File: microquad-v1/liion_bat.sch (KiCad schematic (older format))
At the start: 12 parts

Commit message: Double checked and hooked up connections for BLE Added Power and Pin 12 LED
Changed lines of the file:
@@
 $Descr A4 11693 8268
 encoding utf-8
-Sheet 5 7
+Sheet 5 8
 Title ""
 Date ""
@@
 $EndComp
 Wire Wire Line
-	5600 2750 5400 2750
-Wire Wire Line
-	5400 2750 5350 2750
+	5600 2750 5350 2750
 $Comp
 L C_Small Cbat?
@@
 $EndComp
 Wire Wire Line
-	5600 1800 5600 2250
-Wire Wire Line
-	5600 2250 5600 2750
+	5600 1800 5600 2750
 $Comp
 L GND #PWR019
@@
 $EndComp
 Wire Wire Line
-	5025 3800 5450 3800
-Wire Wire Line
-	5450 3800 5625 3800
+	5025 3800 5625 3800
 Wire Wire Line
 	5625 3800 5625 2950
@@
 	5100 3900 5100 3950
 Wire Wire Line
-	4900 4650 5425 4650
-Wire Wire Line
-	5425 4650 5450 4650
+	4900 4650 5450 4650
 Wire Wire Line
 	5450 4650 5450 3800
@@
 	4900 4850 4975 4850
 Wire Wire Line
-	4975 4850 4975 5025
-Wire Wire Line
-	4975 5025 4975 5075
+	4975 4850 4975 5075
 $Comp
 L R_Small Rbat?
@@
 	4000 4650 3925 4650
 Wire Wire Line
-	3925 4650 3925 4350
-Wire Wire Line
-	3925 4350 3700 4350
-Wire Wire Line
-	3700 4350 3500 4350
+	3925 4350 3925 4650
+Wire Wire Line
+	3500 4350 3925 4350
 $Comp
 L C_Small Cbat?
@@
 Connection ~ 3700 4350
 Wire Wire Line
-	3500 2675 3500 4350
-Wire Wire Line
-	3500 4350 3500 4500
+	3500 2675 3500 4500
 Wire Wire Line
 	3500 4700 3500 4850
@@
 	4250 3150 4250 2950
 Wire Wire Line
-	4250 2950 4375 2950
-Wire Wire Line
-	4375 2950 4450 2950
+	4250 2950 4450 2950
 $Comp
 L GND #PWR027

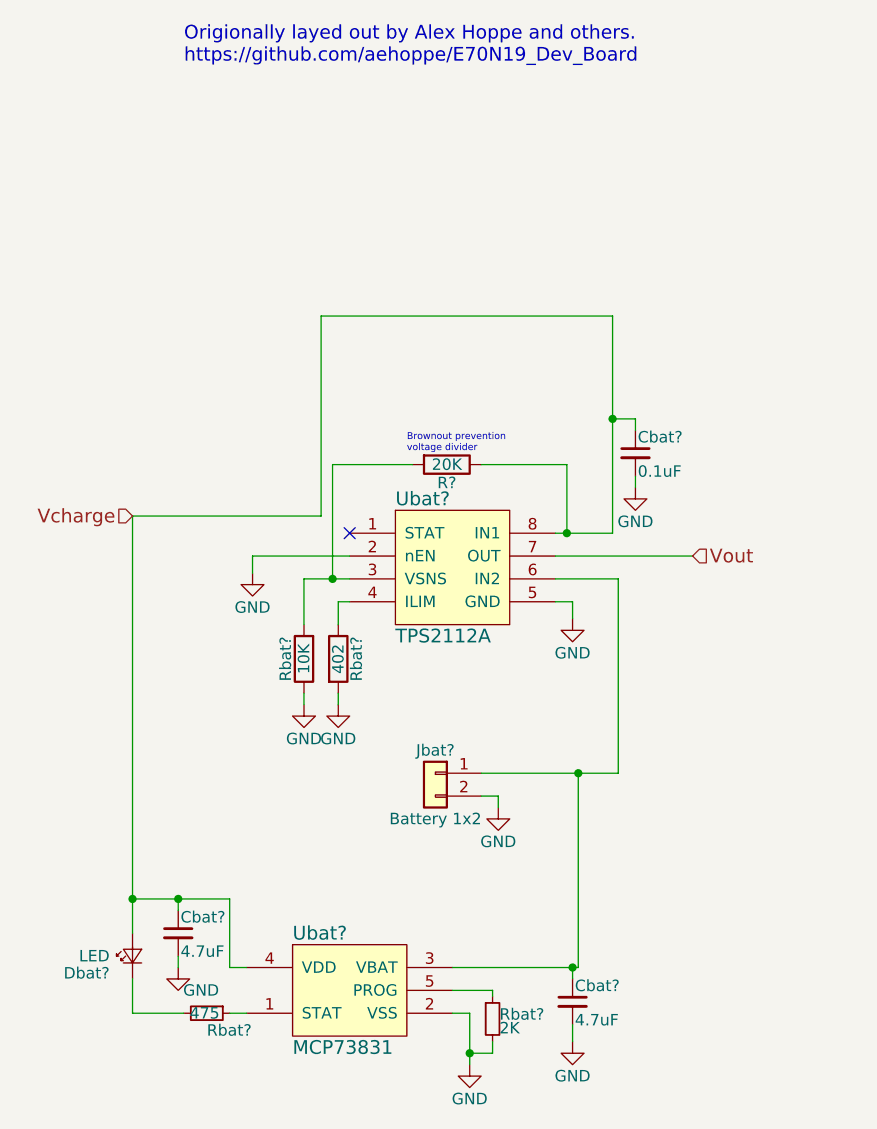
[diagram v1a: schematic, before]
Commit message: Switched battery and merged some more stuff
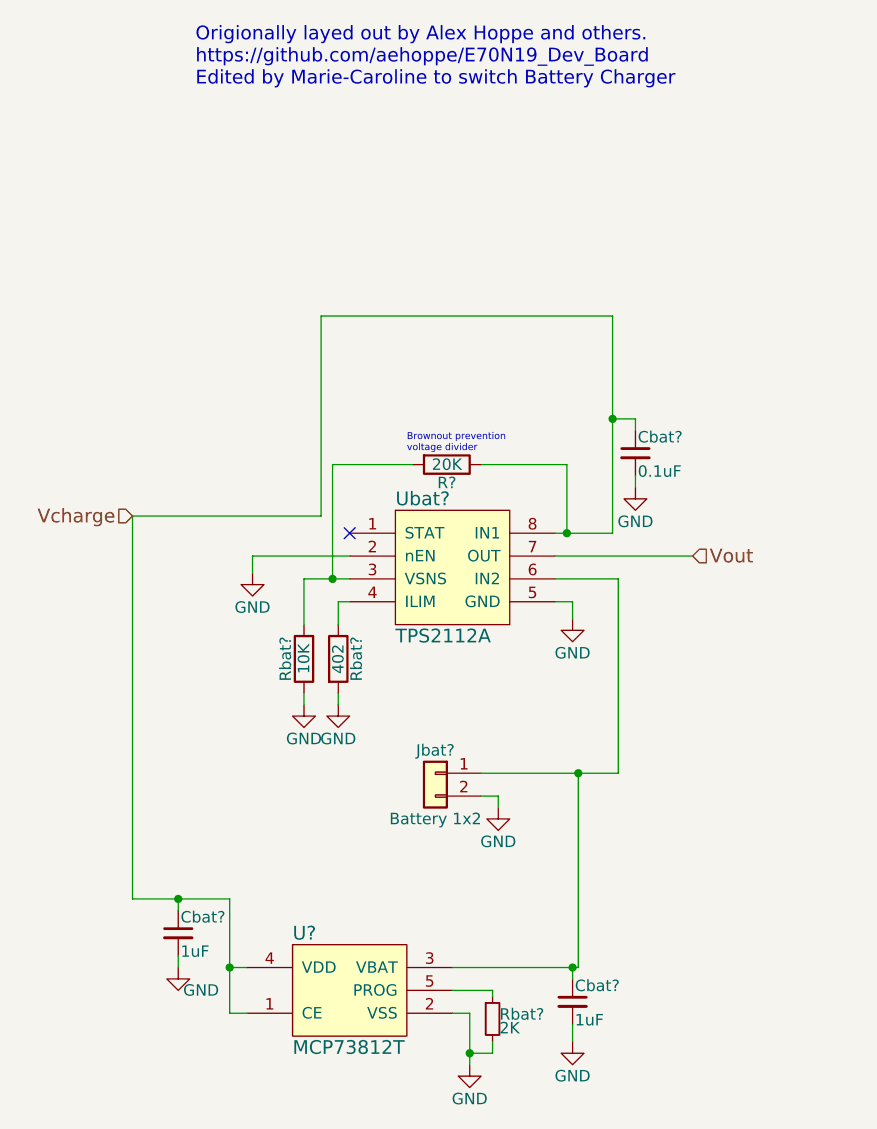
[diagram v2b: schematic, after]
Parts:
- removed Dbat?: LED, LEDs:LED_0805, symbol LED_Small
- removed Rbat?: 475, Resistors_SMD:R_0603, symbol R_Small
- removed Ubat?: MCP73831, TO_SOT_Packages_SMD:SOT-23-5, symbol MCP73831
- added U?: MCP73812T, symbol MCP73812T
- Cbat? (x2): value 4.7uF -> 1uF
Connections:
- net GND: now also U?.2 (VSS)
- net Vcharge: now also U?.1 (CE), U?.4 (VDD)
- net at Cbat?.1, Jbat?.1 (Pin_1), Ubat?.6 (IN2): now also U?.3 (VBAT)
- net at Rbat?.1: now also U?.5 (PROG)
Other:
- note added: "Origionally layed out by Alex Hoppe and others.\nhttps://github.com/aehoppe/E70N19_Dev_Board\nEdited by Marie-Caroline to switch Battery Charger"
- note removed: "Origionally layed out by Alex Hoppe and others.\nhttps://github.com/aehoppe/E70N19_Dev_Board"
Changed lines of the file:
@@
 $Descr A4 11693 8268
 encoding utf-8
-Sheet 5 8
+Sheet 10 8
 Title ""
 Date ""
@@
 U 1 1 59F538F1
 P 4900 2900
+AR Path="/59F6680F/59F538F1" Ref="Ubat?"  Part="1"
+AR Path="/59F56F7F/59F538F1" Ref="Ubat?"  Part="1"
 F 0 "Ubat?" H 4650 3200 60  0000 L CNN
 F 1 "TPS2112A" H 4650 2600 60  0000 L CNN
@@
 U 1 1 59F53938
 P 5700 2400
+AR Path="/59F6680F/59F53938" Ref="Cbat?"  Part="1"
+AR Path="/59F56F7F/59F53938" Ref="Cbat?"  Part="1"
 F 0 "Cbat?" H 5710 2470 50  0000 L CNN
 F 1 "0.1uF" H 5710 2320 50  0000 L CNN
@@
 U 1 1 59F53940
 P 5700 2550
+AR Path="/59F6680F/59F53940" Ref="#PWR019"  Part="1"
+AR Path="/59F56F7F/59F53940" Ref="#PWR019"  Part="1"
 F 0 "#PWR019" H 5700 2300 50  0001 C CNN
 F 1 "GND" H 5700 2400 50  0000 C CNN
@@
 U 1 1 59F5394A
 P 5425 3125
+AR Path="/59F6680F/59F5394A" Ref="#PWR020"  Part="1"
+AR Path="/59F56F7F/59F5394A" Ref="#PWR020"  Part="1"
 F 0 "#PWR020" H 5425 2875 50  0001 C CNN
 F 1 "GND" H 5425 2975 50  0000 C CNN
@@
 U 1 1 59F53953
 P 4400 3500
+AR Path="/59F6680F/59F53953" Ref="#PWR021"  Part="1"
+AR Path="/59F56F7F/59F53953" Ref="#PWR021"  Part="1"
 F 0 "#PWR021" H 4400 3250 50  0001 C CNN
 F 1 "GND" H 4400 3350 50  0000 C CNN
@@
 U 1 1 59F5395B
 P 4400 3300
+AR Path="/59F6680F/59F5395B" Ref="Rbat?"  Part="1"
+AR Path="/59F56F7F/59F5395B" Ref="Rbat?"  Part="1"
 F 0 "Rbat?" V 4480 3300 50  0000 C CNN
 F 1 "402" V 4400 3300 50  0000 C CNN
@@
 	4400 3050 4400 3150
 $Comp
-L MCP73831 Ubat?
-U 1 1 59F53965
-P 4450 4750
-F 0 "Ubat?" H 4200 5000 60  0000 L CNN
-F 1 "MCP73831" H 4200 4500 60  0000 L CNN
-F 2 "TO_SOT_Packages_SMD:SOT-23-5" H 4450 4750 60  0001 C CNN
-F 3 "" H 4450 4750 60  0001 C CNN
-	1    4450 4750
-	1    0    0    -1
-$EndComp
-$Comp
 L Conn_01x02 Jbat?
 U 1 1 59F5396D
 P 4825 3800
+AR Path="/59F6680F/59F5396D" Ref="Jbat?"  Part="1"
+AR Path="/59F56F7F/59F5396D" Ref="Jbat?"  Part="1"
 F 0 "Jbat?" H 4825 3900 50  0000 C CNN
 F 1 "Battery 1x2" H 4825 3600 50  0000 C CNN
@@
 U 1 1 59F53974
 P 5100 3950
+AR Path="/59F6680F/59F53974" Ref="#PWR022"  Part="1"
+AR Path="/59F56F7F/59F53974" Ref="#PWR022"  Part="1"
 F 0 "#PWR022" H 5100 3700 50  0001 C CNN
 F 1 "GND" H 5100 3800 50  0000 C CNN
@@
 U 1 1 59F53983
 P 5425 4800
+AR Path="/59F6680F/59F53983" Ref="Cbat?"  Part="1"
+AR Path="/59F56F7F/59F53983" Ref="Cbat?"  Part="1"
 F 0 "Cbat?" H 5435 4870 50  0000 L CNN
-F 1 "4.7uF" H 5435 4720 50  0000 L CNN
+F 1 "1uF" H 5435 4720 50  0000 L CNN
 F 2 "Capacitors_SMD:C_0603" H 5425 4800 50  0001 C CNN
 F 3 "" H 5425 4800 50  0001 C CNN
@@
 U 1 1 59F5398C
 P 5425 4975
+AR Path="/59F6680F/59F5398C" Ref="#PWR023"  Part="1"
+AR Path="/59F56F7F/59F5398C" Ref="#PWR023"  Part="1"
 F 0 "#PWR023" H 5425 4725 50  0001 C CNN
 F 1 "GND" H 5425 4825 50  0000 C CNN
@@
 U 1 1 59F53993
 P 4975 5075
+AR Path="/59F6680F/59F53993" Ref="#PWR024"  Part="1"
+AR Path="/59F56F7F/59F53993" Ref="#PWR024"  Part="1"
 F 0 "#PWR024" H 4975 4825 50  0001 C CNN
 F 1 "GND" H 4975 4925 50  0000 C CNN
@@
 U 1 1 59F5399C
 P 5075 4875
+AR Path="/59F6680F/59F5399C" Ref="Rbat?"  Part="1"
+AR Path="/59F56F7F/59F5399C" Ref="Rbat?"  Part="1"
 F 0 "Rbat?" H 5105 4895 50  0000 L CNN
 F 1 "2K" H 5105 4835 50  0000 L CNN
@@
 	5075 5025 4975 5025
 Connection ~ 4975 5025
-$Comp
-L LED_Small Dbat?
-U 1 1 59F539A8
-P 3500 4600
-F 0 "Dbat?" V 3425 4700 50  0000 L CNN
-F 1 "LED" V 3500 4700 50  0000 L CNN
-F 2 "LEDs:LED_0805" V 3500 4600 50  0001 C CNN
-F 3 "" V 3500 4600 50  0001 C CNN
-	1    3500 4600
-	0    -1   -1   0
-$EndComp
-$Comp
-L R_Small Rbat?
-U 1 1 59F539B0
-P 3825 4850
-F 0 "Rbat?" V 3900 4850 50  0000 L CNN
-F 1 "475" V 3825 4775 50  0000 L CNN
-F 2 "Resistors_SMD:R_0603" H 3825 4850 50  0001 C CNN
-F 3 "" H 3825 4850 50  0001 C CNN
-F 4 "Value" H 3825 4850 60  0001 C CNN "Fieldname"
-	1    3825 4850
-	0    1    1    0
-$EndComp
-Wire Wire Line
-	3500 4850 3725 4850
-Wire Wire Line
-	3925 4850 4000 4850
 Wire Wire Line
 	4000 4650 3925 4650
 Wire Wire Line
-	3925 4350 3925 4650
-Wire Wire Line
-	3500 4350 3925 4350
+	3925 4350 3925 4850
+Wire Wire Line
+	3925 4350 3500 4350
 $Comp
 L C_Small Cbat?
 U 1 1 59F539BD
 P 3700 4500
+AR Path="/59F6680F/59F539BD" Ref="Cbat?"  Part="1"
+AR Path="/59F56F7F/59F539BD" Ref="Cbat?"  Part="1"
 F 0 "Cbat?" H 3710 4570 50  0000 L CNN
-F 1 "4.7uF" H 3710 4420 50  0000 L CNN
+F 1 "1uF" H 3710 4420 50  0000 L CNN
 F 2 "Capacitors_SMD:C_0603" H 3700 4500 50  0001 C CNN
 F 3 "" H 3700 4500 50  0001 C CNN
@@
 U 1 1 59F539C4
 P 3700 4650
+AR Path="/59F6680F/59F539C4" Ref="#PWR025"  Part="1"
+AR Path="/59F56F7F/59F539C4" Ref="#PWR025"  Part="1"
 F 0 "#PWR025" H 3700 4400 50  0001 C CNN
 F 1 "GND" H 3800 4550 50  0000 C CNN
@@
 Connection ~ 3700 4350
 Wire Wire Line
-	3500 2675 3500 4500
-Wire Wire Line
-	3500 4700 3500 4850
-Connection ~ 3500 4350
-Wire Wire Line
 	4325 1800 4325 2675
 Wire Wire Line
@@
 U 1 1 59F53A15
 P 4875 2450
+AR Path="/59F6680F/59F53A15" Ref="R?"  Part="1"
+AR Path="/59F56F7F/59F53A15" Ref="R?"  Part="1"
 F 0 "R?" V 4955 2450 50  0000 C CNN
 F 1 "20K" V 4875 2450 50  0000 C CNN
@@
 U 1 1 59F53A1D
 P 4250 3300
+AR Path="/59F6680F/59F53A1D" Ref="Rbat?"  Part="1"
+AR Path="/59F56F7F/59F53A1D" Ref="Rbat?"  Part="1"
 F 0 "Rbat?" V 4330 3300 50  0000 C CNN
 F 1 "10K" V 4250 3300 50  0000 C CNN
@@
 U 1 1 59F53A24
 P 4025 2925
+AR Path="/59F6680F/59F53A24" Ref="#PWR026"  Part="1"
+AR Path="/59F56F7F/59F53A24" Ref="#PWR026"  Part="1"
 F 0 "#PWR026" H 4025 2675 50  0001 C CNN
 F 1 "GND" H 4025 2775 50  0000 C CNN
@@
 U 1 1 59F53A2D
 P 4250 3500
+AR Path="/59F6680F/59F53A2D" Ref="#PWR027"  Part="1"
+AR Path="/59F56F7F/59F53A2D" Ref="#PWR027"  Part="1"
 F 0 "#PWR027" H 4250 3250 50  0001 C CNN
 F 1 "GND" H 4250 3350 50  0000 C CNN
@@
 Text HLabel 3500 2675 0    60   Input ~ 0
 Vcharge
-Text Notes 3725 700  0    60   ~ 0
-Origionally layed out by Alex Hoppe and others.\nhttps://github.com/aehoppe/E70N19_Dev_Board
+Text Notes 3775 800  0    60   ~ 0
+Origionally layed out by Alex Hoppe and others.\nhttps://github.com/aehoppe/E70N19_Dev_Board\nEdited by Marie-Caroline to switch Battery Charger
+$Comp
+L MCP73812T U?
+U 1 1 59F66E7B
+P 4450 4750
+F 0 "U?" H 4200 5000 60  0000 L CNN
+F 1 "MCP73812T" H 4200 4500 60  0000 L CNN
+F 2 "" H 4450 4750 60  0001 C CNN
+F 3 "" H 4450 4750 60  0001 C CNN
+	1    4450 4750
+	1    0    0    -1
+$EndComp
+Wire Wire Line
+	3925 4850 4000 4850
+Connection ~ 3925 4650
+Wire Wire Line
+	3500 2675 3500 4350
 $EndSCHEMATC
